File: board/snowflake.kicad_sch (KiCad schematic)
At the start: 68 parts, among them J1 Conn_01x02_Pin, J3 TC2030, U1 TZ-5050S2RGB-5V-I4-H1, U10 TZ-5050S2RGB-5V-I4-H1, U11 TZ-5050S2RGB-5V-I4-H1, U12 TZ-5050S2RGB-5V-I4-H1, U13 TZ-5050S2RGB-5V-I4-H1, U14 TZ-5050S2RGB-5V-I4-H1, U15 TZ-5050S2RGB-5V-I4-H1, U16 TZ-5050S2RGB-5V-I4-H1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

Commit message: Final board updates before sending
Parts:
- removed R0: 510k, Resistor_SMD:R_0603_1608Metric, symbol Device:R
- C66: footprint snowflake:C_0402_1005Metric -> Capacitor_SMD:C_0603_1608Metric; LCSC C1525 -> C14663; MPN C1525 -> (none)
- R1: value 220k -> 732k
- TP5, TP6, TP7: footprint snowflake:TestPoint_Pad_D2.0mm -> snowflake:TouchPad
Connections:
- net BAT+: now also S1.1; no longer S1.3
- net FB: now also R1.1
- net GND: now also S1.3; no longer S1.1
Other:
- note added: "(732k/100k + 1) * 0.6 = 5v"
- note removed: "((510k + 220k)/100k + 1) * 0.6 = 4.98v"
- moved on the sheet: S1
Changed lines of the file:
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@@
 		)
 	)
-	(text "((510k + 220k)/100k + 1) * 0.6\n  = 4.98v"
+	(text "(732k/100k + 1) * 0.6\n  = 5v"
 		(exclude_from_sim no)
-		(at 99.568 57.404 0)
+		(at 136.906 55.372 0)
 		(effects
 			(font
@@
 	)
 	(junction
-		(at 38.1 36.83)
-		(diameter 0)
-		(color 0 0 0 0)
-	)
-	(junction
 		(at 210.82 105.41)
 		(diameter 0)
@@
 	)
 	(junction
+		(at 53.34 36.83)
+		(diameter 0)
+		(color 0 0 0 0)
+	)
+	(junction
 		(at 120.65 43.18)
 		(diameter 0)
@@
 	(wire
 		(pts
-			(xy 40.64 39.37) (xy 38.1 36.83)
+			(xy 50.8 39.37) (xy 53.34 36.83)
 		)
 		(stroke
@@
 	(wire
 		(pts
-			(xy 34.29 36.83) (xy 34.29 40.64)
+			(xy 54.61 36.83) (xy 54.61 40.64)
 		)
 		(stroke
@@
 	(wire
 		(pts
-			(xy 43.18 30.48) (xy 35.56 30.48)
-		)
-		(stroke
-			(width 0)
-			(type default)
-		)
-	)
-	(wire
-		(pts
 			(xy 48.26 30.48) (xy 54.61 30.48)
 		)
@@
 	(wire
 		(pts
+			(xy 35.56 30.48) (xy 43.18 30.48)
+		)
+		(stroke
+			(width 0)
+			(type default)
+		)
+	)
+	(wire
+		(pts
 			(xy 256.54 102.87) (xy 256.54 105.41)
 		)
@@
 	(wire
 		(pts
-			(xy 38.1 36.83) (xy 40.64 36.83)
+			(xy 53.34 36.83) (xy 50.8 36.83)
 		)
 		(stroke
@@
 	(wire
 		(pts
-			(xy 34.29 36.83) (xy 38.1 36.83)
+			(xy 30.48 120.65) (xy 30.48 123.19)
 		)
 		(stroke
@@
 	(wire
 		(pts
-			(xy 30.48 120.65) (xy 30.48 123.19)
+			(xy 124.46 113.03) (xy 142.24 113.03)
 		)
 		(stroke
@@
 	(wire
 		(pts
-			(xy 124.46 113.03) (xy 142.24 113.03)
+			(xy 165.1 259.08) (xy 165.1 265.43)
 		)
 		(stroke
@@
 	(wire
 		(pts
-			(xy 165.1 259.08) (xy 165.1 265.43)
+			(xy 142.24 95.25) (xy 142.24 105.41)
 		)
 		(stroke
@@
 	(wire
 		(pts
-			(xy 142.24 95.25) (xy 142.24 105.41)
+			(xy 53.34 36.83) (xy 54.61 36.83)
 		)
 		(stroke
@@
 	(wire
 		(pts
+			(xy 120.65 50.8) (xy 120.65 58.42)
+		)
+		(stroke
+			(width 0)
+			(type default)
+		)
+	)
+	(wire
+		(pts
 			(xy 95.25 189.23) (xy 95.25 196.85)
 		)
@@
 			)
 		)
-		(property "Footprint" "snowflake:C_0402_1005Metric"
+		(property "Footprint" "Capacitor_SMD:C_0603_1608Metric"
 			(at 106.68 195.8848 0)
 			(effects
@@
 			)
 		)
-		(property "LCSC" "C1525"
-			(at 102.87 196.85 0)
-			(effects
-				(font
-					(size 1.27 1.27)
-				)
-				(hide yes)
-			)
-		)
-		(property "MPN" "C1525"
+		(property "LCSC" "C14663"
 			(at 102.87 196.85 0)
 			(effects
@@
 			)
 		)
-		(property "Footprint" "snowflake:TestPoint_Pad_D2.0mm"
+		(property "Footprint" "snowflake:TouchPad"
 			(at 176.53 267.97 0)
 			(effects
@@
 			)
 		)
-		(property "Footprint" "snowflake:TestPoint_Pad_D2.0mm"
+		(property "Footprint" "snowflake:TouchPad"
 			(at 176.53 273.05 0)
 			(effects
@@
 	(symbol
 		(lib_id "power:GND")
-		(at 34.29 40.64 0)
+		(at 54.61 40.64 0)
+		(mirror y)
 		(unit 1)
 		(exclude_from_sim no)
@@
 		(dnp no)
 		(property "Reference" "#PWR03"
-			(at 34.29 46.99 0)
+			(at 54.61 46.99 0)
 			(effects
 				(font
@@
 		)
 		(property "Value" "GND"
-			(at 35.814 40.132 0)
+			(at 60.198 39.37 0)
 			(effects
 				(font
@@
 		)
 		(property "Footprint" ""
-			(at 34.29 40.64 0)
+			(at 54.61 40.64 0)
 			(effects
 				(font
@@
 		)
 		(property "Datasheet" ""
-			(at 34.29 40.64 0)
+			(at 54.61 40.64 0)
 			(effects
 				(font
@@
 		)
 		(property "Description" "Power symbol creates a global label with name \"GND\" , ground"
-			(at 34.29 40.64 0)
+			(at 54.61 40.64 0)
 			(effects
 				(font
@@
 			)
 		)
-		(property "Value" "220k"
+		(property "Value" "732k"
 			(at 122.936 46.99 90)
 			(effects
@@
 	)
 	(symbol
-		(lib_id "Device:R")
-		(at 120.65 54.61 0)
-		(unit 1)
-		(exclude_from_sim no)
-		(in_bom yes)
-		(on_board yes)
-		(dnp no)
-		(property "Reference" "R0"
-			(at 124.968 54.61 90)
-			(effects
-				(font
-					(size 1.016 1.016)
-				)
-			)
-		)
-		(property "Value" "510k"
-			(at 122.936 54.61 90)
-			(effects
-				(font
-					(size 1.27 1.27)
-				)
-			)
-		)
-		(property "Footprint" "Resistor_SMD:R_0603_1608Metric"
-			(at 118.872 54.61 90)
-			(effects
-				(font
-					(size 1.27 1.27)
-				)
-				(hide yes)
-			)
-		)
-		(property "Datasheet" "~"
-			(at 120.65 54.61 0)
-			(effects
-				(font
-					(size 1.27 1.27)
-				)
-				(hide yes)
-			)
-		)
-		(property "Description" "Resistor"
-			(at 120.65 54.61 0)
-			(effects
-				(font
-					(size 1.27 1.27)
-				)
-				(hide yes)
-			)
-		)
-		(property "LCSC" "C23192"
-			(at 124.968 54.61 0)
-			(effects
-				(font
-					(size 1.27 1.27)
-				)
-				(hide yes)
-			)
-		)
-		(pin "1"
-		)
-		(pin "2"
-		)
-		(instances
-			(project ""
-				(path "/40481058-4523-4575-8fee-da98fa47c16e"
-					(reference "R0")
-					(unit 1)
-				)
-			)
-		)
-	)
-	(symbol
 		(lib_id "power:+5V")
 		(at 30.48 120.65 0)
@@
 			)
 		)
-		(property "Footprint" "snowflake:TestPoint_Pad_D2.0mm"
+		(property "Footprint" "snowflake:TouchPad"
 			(at 176.53 270.51 0)
 			(effects
@@
 	(symbol
 		(lib_id "Digikey:SLW-1277545-3A-RA-N-D")
-		(at 45.72 35.56 270)
-		(mirror x)
+		(at 45.72 35.56 90)
 		(unit 1)
 		(exclude_from_sim no)
@@
 		(dnp no)
 		(property "Reference" "S1"
-			(at 50.8 38.1 0)
+			(at 40.64 38.1 0)
 			(effects
 				(font
@@
 		)
 		(property "Value" "SLW-1277545-3A-RA-N-D"
-			(at 40.64 40.64 0)
+			(at 50.8 40.64 0)
 			(effects
 				(font

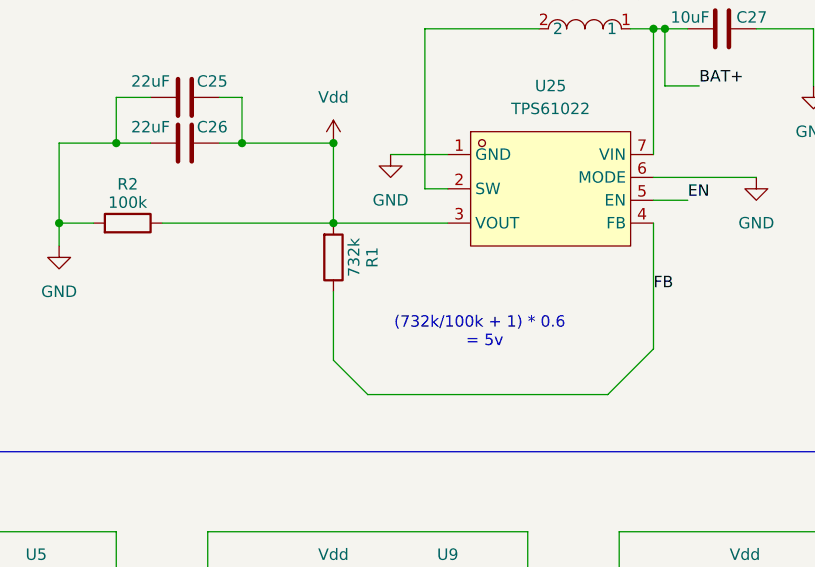
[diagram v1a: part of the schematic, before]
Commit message: Catch what would have been a huge mistake
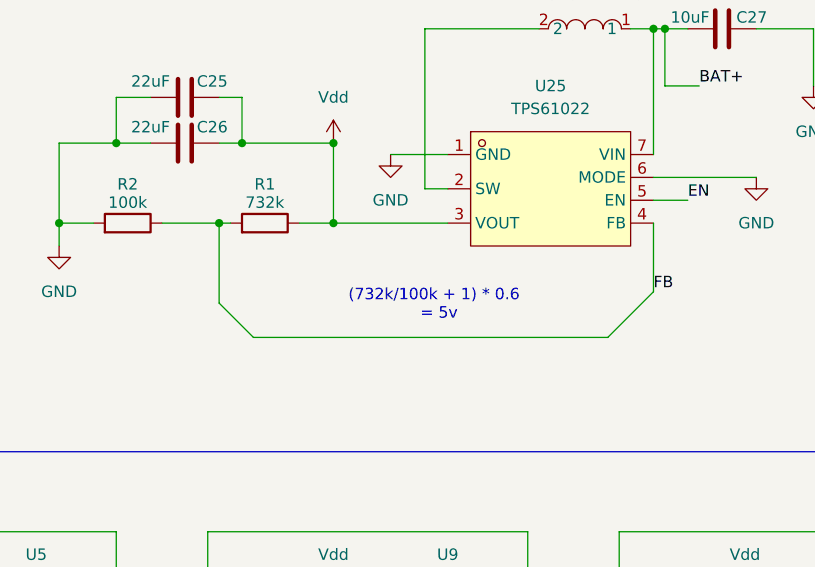
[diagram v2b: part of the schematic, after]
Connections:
- net FB: now also R1.2, R2.1; no longer R1.1
- net Vdd: now also R1.1; no longer R1.2, R2.1
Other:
- moved on the sheet: R1
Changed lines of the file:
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@@
 	(text "(732k/100k + 1) * 0.6\n  = 5v"
 		(exclude_from_sim no)
-		(at 136.906 55.372 0)
+		(at 131.826 52.324 0)
 		(effects
 			(font
@@
 	)
 	(junction
+		(at 107.95 43.18)
+		(diameter 0)
+		(color 0 0 0 0)
+	)
+	(junction
 		(at 256.54 87.63)
 		(diameter 0)
@@
 	(wire
 		(pts
-			(xy 120.65 43.18) (xy 133.35 43.18)
-		)
-		(stroke
-			(width 0)
-			(type default)
-		)
-	)
-	(wire
-		(pts
 			(xy 113.03 140.97) (xy 113.03 144.78)
 		)
@@
 	(wire
 		(pts
-			(xy 101.6 43.18) (xy 120.65 43.18)
+			(xy 101.6 43.18) (xy 107.95 43.18)
 		)
 		(stroke
@@
 	(wire
 		(pts
-			(xy 156.21 57.15) (xy 151.13 62.23)
+			(xy 156.21 50.8) (xy 151.13 55.88)
 		)
 		(stroke
@@
 	(wire
 		(pts
+			(xy 107.95 43.18) (xy 107.95 52.07)
+		)
+		(stroke
+			(width 0)
+			(type default)
+		)
+	)
+	(wire
+		(pts
 			(xy 127 35.56) (xy 133.35 35.56)
 		)
@@
 	(wire
 		(pts
-			(xy 151.13 62.23) (xy 124.46 62.23)
+			(xy 151.13 55.88) (xy 111.76 55.88)
 		)
 		(stroke
@@
 	(wire
 		(pts
+			(xy 107.95 43.18) (xy 109.22 43.18)
+		)
+		(stroke
+			(width 0)
+			(type default)
+		)
+	)
+	(wire
+		(pts
 			(xy 120.65 85.09) (xy 120.65 87.63)
 		)
@@
 	(wire
 		(pts
-			(xy 156.21 43.18) (xy 156.21 57.15)
+			(xy 156.21 43.18) (xy 156.21 50.8)
 		)
 		(stroke
@@
 	(wire
 		(pts
-			(xy 124.46 62.23) (xy 120.65 58.42)
+			(xy 111.76 55.88) (xy 107.95 52.07)
+		)
+		(stroke
+			(width 0)
+			(type default)
+		)
+	)
+	(wire
+		(pts
+			(xy 120.65 43.18) (xy 133.35 43.18)
 		)
 		(stroke
@@
 	(wire
 		(pts
+			(xy 116.84 43.18) (xy 120.65 43.18)
+		)
+		(stroke
+			(width 0)
+			(type default)
+		)
+	)
+	(wire
+		(pts
 			(xy 52.07 90.17) (xy 55.88 90.17)
 		)
@@
 	(wire
 		(pts
-			(xy 120.65 50.8) (xy 120.65 58.42)
-		)
-		(stroke
-			(width 0)
-			(type default)
-		)
-	)
-	(wire
-		(pts
 			(xy 95.25 189.23) (xy 95.25 196.85)
 		)
@@
 	(symbol
 		(lib_id "Device:R")
-		(at 120.65 46.99 0)
+		(at 113.03 43.18 270)
 		(mirror x)
 		(unit 1)
@@
 		(dnp no)
 		(property "Reference" "R1"
-			(at 124.968 46.99 90)
+			(at 113.03 38.862 90)
 			(effects
 				(font
@@
 		)
 		(property "Value" "732k"
-			(at 122.936 46.99 90)
+			(at 113.03 40.894 90)
 			(effects
 				(font
@@
 		)
 		(property "Footprint" "Resistor_SMD:R_0603_1608Metric"
-			(at 118.872 46.99 90)
+			(at 113.03 44.958 90)
 			(effects
 				(font
@@
 		)
 		(property "Datasheet" "~"
-			(at 120.65 46.99 0)
+			(at 113.03 43.18 0)
 			(effects
 				(font
@@
 		)
 		(property "Description" "Resistor"
-			(at 120.65 46.99 0)
+			(at 113.03 43.18 0)
 			(effects
 				(font
@@
 		)
 		(property "LCSC" "C22961"
-			(at 120.65 46.99 90)
+			(at 113.03 43.18 90)
 			(effects
 				(font

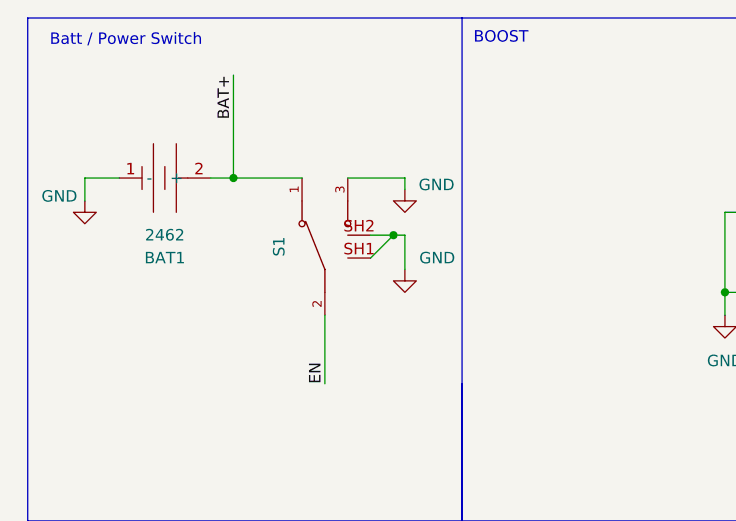
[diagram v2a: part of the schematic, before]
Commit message: Cleanup power switch traces
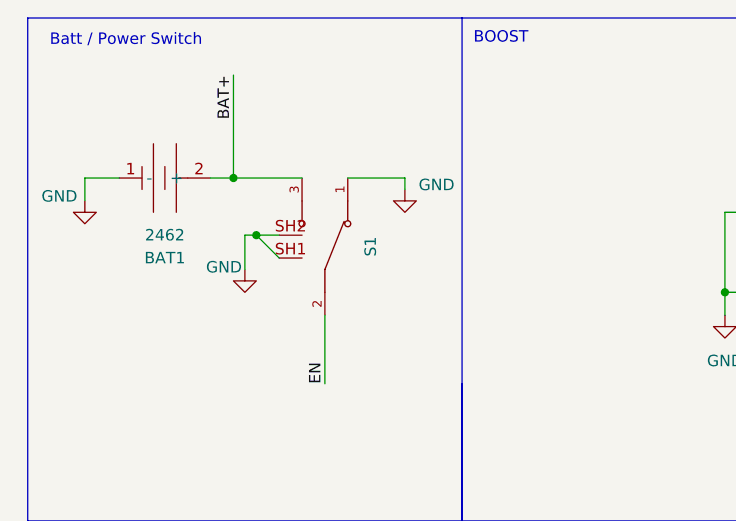
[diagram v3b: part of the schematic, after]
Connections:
- net BAT+: now also S1.3; no longer S1.1
- net GND: now also S1.1; no longer S1.3
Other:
- moved on the sheet: S1
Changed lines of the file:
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@@
 	)
 	(junction
-		(at 53.34 36.83)
+		(at 38.1 36.83)
 		(diameter 0)
 		(color 0 0 0 0)
@@
 	(wire
 		(pts
-			(xy 50.8 39.37) (xy 53.34 36.83)
+			(xy 40.64 39.37) (xy 38.1 36.83)
 		)
 		(stroke
@@
 	(wire
 		(pts
-			(xy 54.61 36.83) (xy 54.61 40.64)
+			(xy 36.83 36.83) (xy 36.83 40.64)
 		)
 		(stroke
@@
 	(wire
 		(pts
-			(xy 48.26 30.48) (xy 54.61 30.48)
-		)
-		(stroke
-			(width 0)
-			(type default)
-		)
-	)
-	(wire
-		(pts
 			(xy 74.93 105.41) (xy 78.74 105.41)
 		)
@@
 	(wire
 		(pts
-			(xy 53.34 36.83) (xy 50.8 36.83)
+			(xy 38.1 36.83) (xy 40.64 36.83)
 		)
 		(stroke
@@
 	(wire
 		(pts
-			(xy 53.34 36.83) (xy 54.61 36.83)
+			(xy 38.1 36.83) (xy 36.83 36.83)
 		)
 		(stroke
@@
 	(wire
 		(pts
+			(xy 48.26 30.48) (xy 54.61 30.48)
+		)
+		(stroke
+			(width 0)
+			(type default)
+		)
+	)
+	(wire
+		(pts
 			(xy 19.05 30.48) (xy 19.05 33.02)
 		)
@@
 	(symbol
 		(lib_id "power:GND")
-		(at 54.61 40.64 0)
-		(mirror y)
+		(at 36.83 40.64 0)
 		(unit 1)
 		(exclude_from_sim no)
@@
 		(dnp no)
 		(property "Reference" "#PWR03"
-			(at 54.61 46.99 0)
+			(at 36.83 46.99 0)
 			(effects
 				(font
@@
 		)
 		(property "Value" "GND"
-			(at 60.198 39.37 0)
+			(at 32.512 40.386 0)
 			(effects
 				(font
@@
 		)
 		(property "Footprint" ""
-			(at 54.61 40.64 0)
+			(at 36.83 40.64 0)
 			(effects
 				(font
@@
 		)
 		(property "Datasheet" ""
-			(at 54.61 40.64 0)
+			(at 36.83 40.64 0)
 			(effects
 				(font
@@
 		)
 		(property "Description" "Power symbol creates a global label with name \"GND\" , ground"
-			(at 54.61 40.64 0)
+			(at 36.83 40.64 0)
 			(effects
 				(font
@@
 	(symbol
 		(lib_id "Digikey:SLW-1277545-3A-RA-N-D")
-		(at 45.72 35.56 90)
+		(at 45.72 35.56 270)
+		(mirror x)
 		(unit 1)
 		(exclude_from_sim no)
@@
 		(dnp no)
 		(property "Reference" "S1"
-			(at 40.64 38.1 0)
+			(at 50.8 38.1 0)
 			(effects
 				(font
@@
 		)
 		(property "Value" "SLW-1277545-3A-RA-N-D"
-			(at 50.8 40.64 0)
+			(at 40.64 40.64 0)
 			(effects
 				(font

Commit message: Add missing 3d file for CH32v003 footprint
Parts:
- U26: footprint Package_DFN_QFN:QFN-20-1EP_3x3mm_P0.4mm_EP1.65x1.65mm -> easyeda2kicad:QFN-20_L3.0-W3.0-P0.40-TL-EP1.7
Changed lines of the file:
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@@
 			)
 		)
-		(property "Footprint" "Package_DFN_QFN:QFN-20-1EP_3x3mm_P0.4mm_EP1.65x1.65mm"
+		(property "Footprint" "easyeda2kicad:QFN-20_L3.0-W3.0-P0.40-TL-EP1.7"
 			(at 87.63 236.22 0)
 			(effects
